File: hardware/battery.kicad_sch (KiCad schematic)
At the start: 10 parts, among them IC1 BQ29732DSER, Q1 CSD16406Q3, Q2 CSD16406Q3

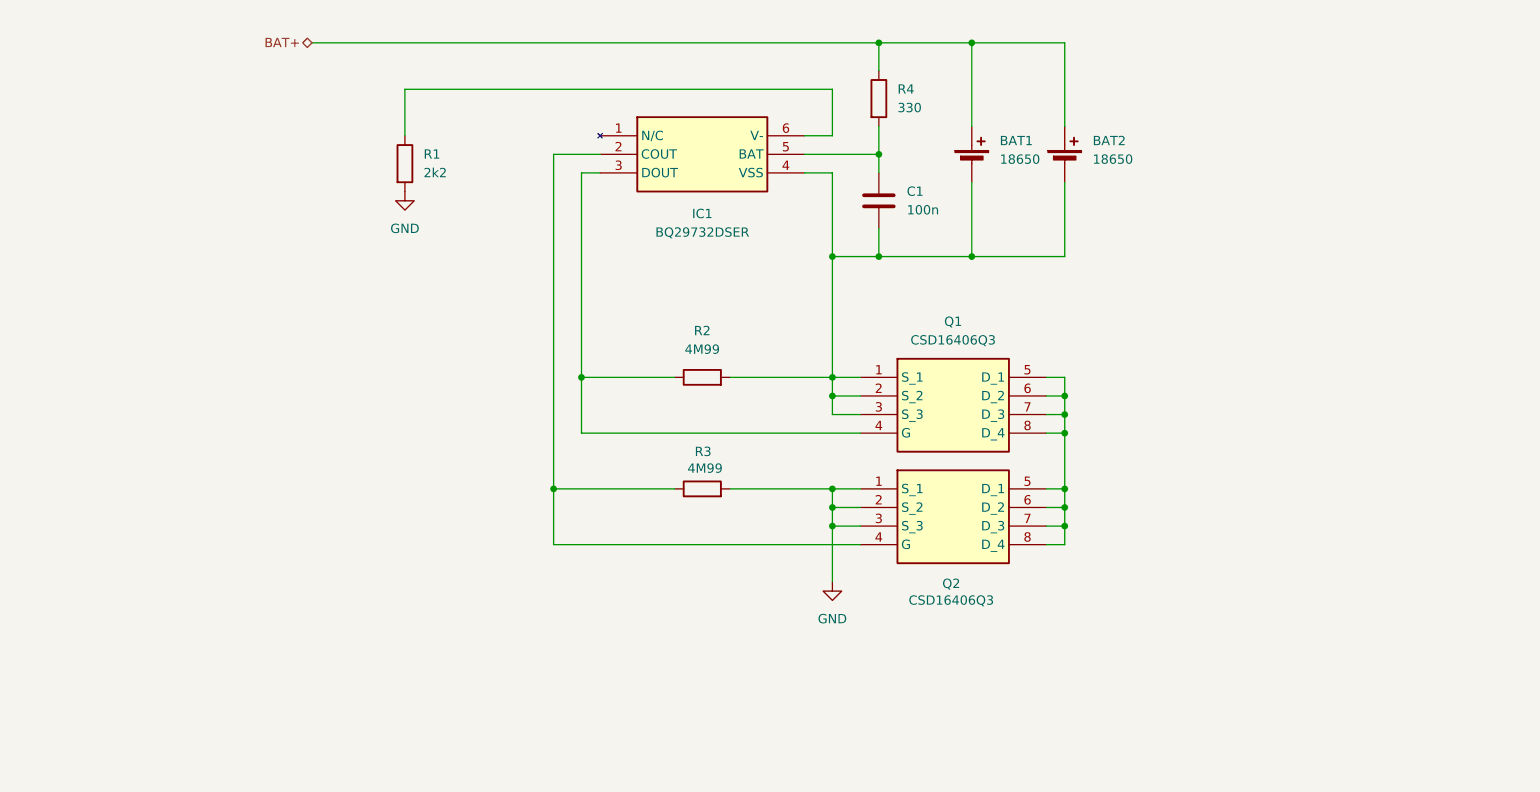
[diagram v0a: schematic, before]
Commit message: Battery temperature meter added to MCU
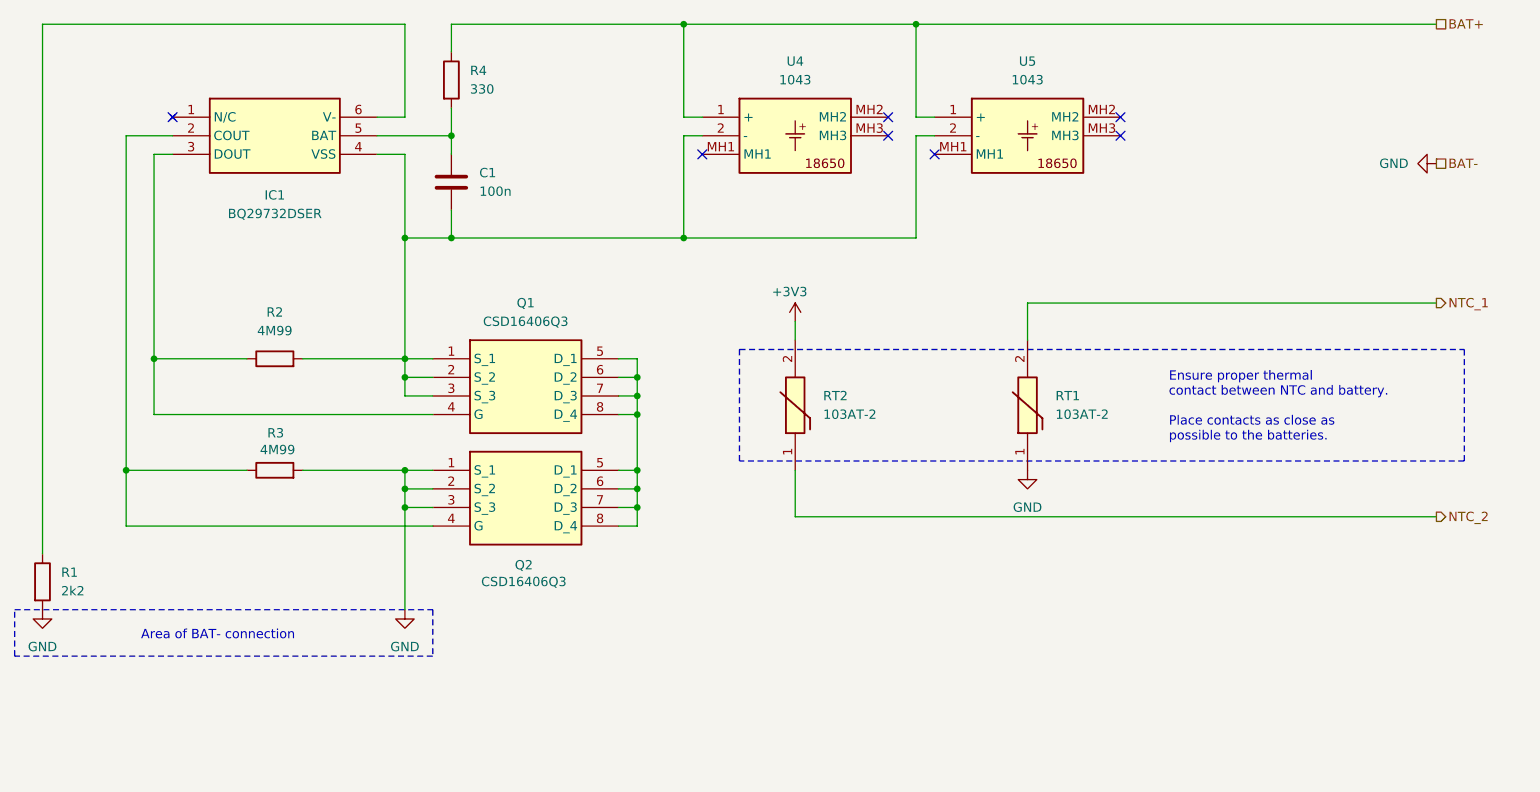
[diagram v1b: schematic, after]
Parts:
- removed BAT1, BAT2: 18650, symbol Device:Battery_Cell
- added RT1, RT2: 103AT-2, 103AT2, symbol SamacSys_Parts:103AT-2
- added U4, U5: 1043, 1043, symbol SamacSys_Parts:1043
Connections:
- net BAT+: now also U4.1 (+), U5.1 (+)
- net GND: now also RT1.1
- net at C1.2, IC1.4 (VSS), Q1.1 (S_1)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: now also U4.2 (-), U5.2 (-)
- new net +3V3: RT2.2
- new net NTC_1: RT1.2
- new net NTC_2: RT2.1
- no-connect marks 0 -> 7
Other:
- note added: "Area of BAT- connection"
- note added: "Ensure proper thermal contact between NTC and battery. Place contacts as close as possible to the batteries."
- moved on the sheet: C1, IC1, Q1, Q2, R1, R2, R3, R4

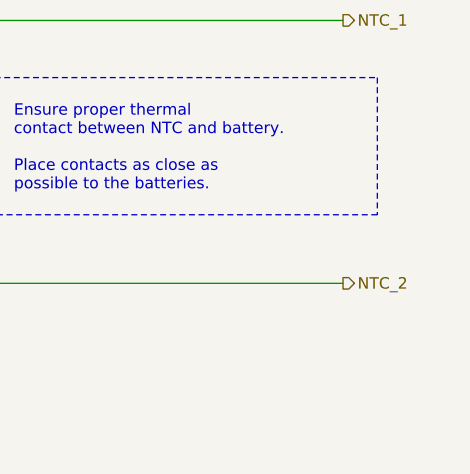
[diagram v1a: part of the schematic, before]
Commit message: Board connector added
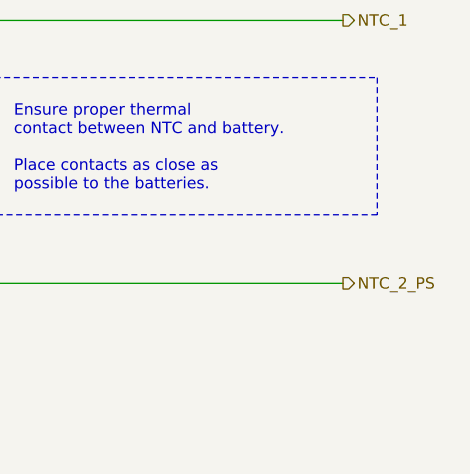
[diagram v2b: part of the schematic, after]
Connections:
- net NTC_2 renamed NTC_2_PS
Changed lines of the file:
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@@
 		)
 	)
-	(hierarchical_label "NTC_2"
+	(hierarchical_label "NTC_2_PS"
 		(shape output)
 		(at 245.11 124.46 0)

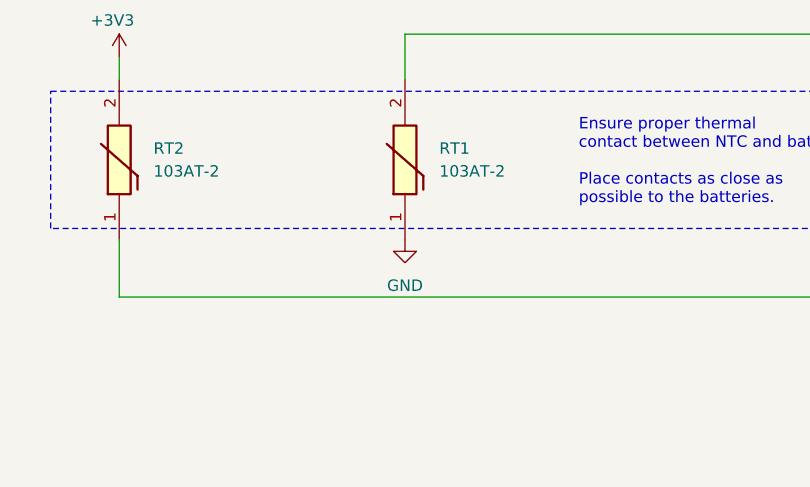
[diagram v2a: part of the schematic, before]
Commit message: Fixed MOS and board connector
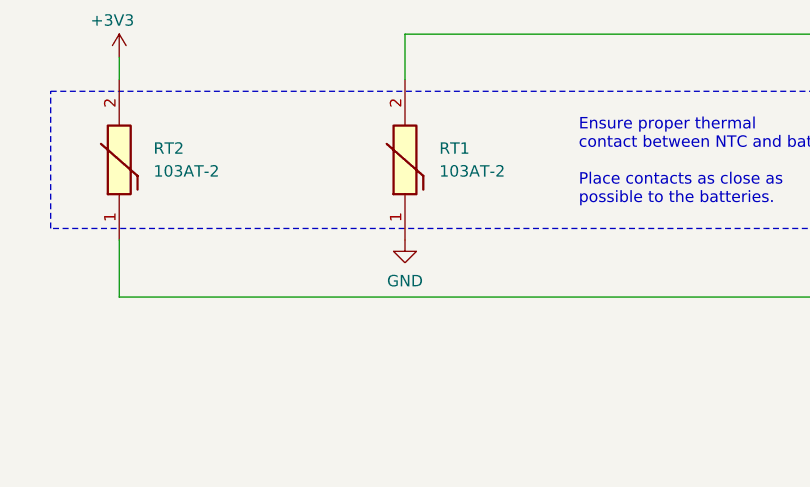
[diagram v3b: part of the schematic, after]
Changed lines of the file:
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@@
 		(on_board yes)
 		(dnp no)
-		(fields_autoplaced yes)
 		(property "Reference" "#PWR073"
 			(at 189.23 124.46 0)
@@
 		)
 		(property "Value" "GND"
-			(at 189.23 123.19 0)
+			(at 189.23 122.682 0)
 			(effects
 				(font

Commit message: prevention save
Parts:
- C1: footprint (none) -> Capacitor_SMD:C_0402_1005Metric
- R1: renamed from R4; footprint Resistor_SMD:R_0805_2012Metric -> Resistor_SMD:R_0603_1608Metric
- R4: renamed from R1; footprint Resistor_SMD:R_0805_2012Metric -> Resistor_SMD:R_0402_1005Metric
- renumbered U4 to BAT1, U5 to BAT2
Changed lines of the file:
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@@
 		(dnp no)
 		(fields_autoplaced yes)
-		(property "Reference" "R1"
+		(property "Reference" "R4"
 			(at 57.15 132.0799 0)
 			(effects
@@
 			)
 		)
-		(property "Footprint" "Resistor_SMD:R_0805_2012Metric"
+		(property "Footprint" "Resistor_SMD:R_0402_1005Metric"
 			(at 52.832 133.35 90)
 			(effects
@@
 			(project "obvod"
 				(path "/e8e834c4-1afb-42f7-b718-3cb720dae1d5/f61c7da5-11ee-4b50-a688-248a75ac3e8f"
-					(reference "R1")
+					(reference "R4")
 					(unit 1)
 				)
@@
 		(dnp no)
 		(fields_autoplaced yes)
-		(property "Reference" "U4"
+		(property "Reference" "BAT1"
 			(at 157.48 62.23 0)
 			(effects
@@
 			(project ""
 				(path "/e8e834c4-1afb-42f7-b718-3cb720dae1d5/f61c7da5-11ee-4b50-a688-248a75ac3e8f"
-					(reference "U4")
+					(reference "BAT1")
 					(unit 1)
 				)
@@
 		(dnp no)
 		(fields_autoplaced yes)
-		(property "Reference" "U5"
+		(property "Reference" "BAT2"
 			(at 189.23 62.23 0)
 			(effects
@@
 			(project "obvod"
 				(path "/e8e834c4-1afb-42f7-b718-3cb720dae1d5/f61c7da5-11ee-4b50-a688-248a75ac3e8f"
-					(reference "U5")
+					(reference "BAT2")
 					(unit 1)
 				)
@@
 			)
 		)
-		(property "Footprint" ""
+		(property "Footprint" "Capacitor_SMD:C_0402_1005Metric"
 			(at 111.4552 82.55 0)
 			(effects
@@
 		(dnp no)
 		(fields_autoplaced yes)
-		(property "Reference" "R4"
+		(property "Reference" "R1"
 			(at 113.03 63.4999 0)
 			(effects
@@
 			)
 		)
-		(property "Footprint" "Resistor_SMD:R_0805_2012Metric"
+		(property "Footprint" "Resistor_SMD:R_0603_1608Metric"
 			(at 108.712 64.77 90)
 			(effects
@@
 			(project "obvod"
 				(path "/e8e834c4-1afb-42f7-b718-3cb720dae1d5/f61c7da5-11ee-4b50-a688-248a75ac3e8f"
-					(reference "R4")
+					(reference "R1")
 					(unit 1)
 				)

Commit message: Revised and completed BOM
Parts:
- R2, R3: footprint Resistor_SMD:R_0805_2012Metric -> Resistor_SMD:R_0402_1005Metric
- renumbered RT1 to NTC1, RT2 to NTC2
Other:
- moved on the sheet: NTC1, NTC2
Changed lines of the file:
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@@
 	(wire
 		(pts
-			(xy 157.48 97.79) (xy 157.48 100.33)
+			(xy 189.23 132.08) (xy 189.23 134.62)
 		)
 		(stroke
@@
 	(wire
 		(pts
+			(xy 189.23 158.75) (xy 245.11 158.75)
+		)
+		(stroke
+			(width 0)
+			(type default)
+		)
+	)
+	(wire
+		(pts
 			(xy 135.89 125.73) (xy 135.89 123.19)
 		)
@@
 	(wire
 		(pts
-			(xy 189.23 95.25) (xy 189.23 100.33)
+			(xy 189.23 93.98) (xy 189.23 99.06)
 		)
 		(stroke
@@
 	(wire
 		(pts
-			(xy 245.11 124.46) (xy 157.48 124.46)
-		)
-		(stroke
-			(width 0)
-			(type default)
-		)
-	)
-	(wire
-		(pts
 			(xy 69.85 102.87) (xy 82.55 102.87)
 		)
@@
 	(wire
 		(pts
-			(xy 245.11 95.25) (xy 189.23 95.25)
+			(xy 245.11 93.98) (xy 189.23 93.98)
 		)
 		(stroke
@@
 	(wire
 		(pts
-			(xy 157.48 124.46) (xy 157.48 118.11)
+			(xy 189.23 158.75) (xy 189.23 152.4)
 		)
 		(stroke
@@
 	)
 	(rectangle
-		(start 149.86 101.6)
-		(end 248.92 116.84)
+		(start 182.88 100.33)
+		(end 248.92 153.67)
 		(stroke
 			(width 0)
@@
 	(text "Ensure proper thermal \ncontact between NTC and battery.\n\nPlace contacts as close as \npossible to the batteries."
 		(exclude_from_sim no)
-		(at 208.534 109.474 0)
+		(at 208.788 127 0)
 		(effects
 			(font
@@
 	(hierarchical_label "NTC_2_PS"
 		(shape output)
-		(at 245.11 124.46 0)
+		(at 245.11 158.75 0)
 		(effects
 			(font
@@
 	(hierarchical_label "NTC_1"
 		(shape output)
-		(at 245.11 95.25 0)
+		(at 245.11 93.98 0)
 		(effects
 			(font
@@
 	(symbol
 		(lib_id "SamacSys_Parts:103AT-2")
-		(at 157.48 118.11 90)
+		(at 189.23 152.4 90)
 		(unit 1)
 		(exclude_from_sim no)
@@
 		(dnp no)
 		(fields_autoplaced yes)
-		(property "Reference" "RT2"
-			(at 161.29 107.9499 90)
+		(property "Reference" "NTC2"
+			(at 193.04 142.2399 90)
 			(effects
 				(font
@@
 		)
 		(property "Value" "103AT-2"
-			(at 161.29 110.4899 90)
+			(at 193.04 144.7799 90)
 			(effects
 				(font
@@
 		)
 		(property "Footprint" "103AT2"
-			(at 253.67 104.14 0)
+			(at 285.42 138.43 0)
 			(effects
 				(font
@@
 		)
 		(property "Datasheet" "https://www.semitec-global.com/uploads/2022/01/P12-13-AT-Thermistor.pdf"
-			(at 353.67 104.14 0)
+			(at 385.42 138.43 0)
 			(effects
 				(font
@@
 		)
 		(property "Description" "NTC (Negative Temperature Coefficient) Thermistors 10kohm 1%"
-			(at 157.48 118.11 0)
+			(at 189.23 152.4 0)
 			(effects
 				(font
@@
 		)
 		(property "Height" "9.5"
-			(at 553.67 104.14 0)
+			(at 585.42 138.43 0)
 			(effects
 				(font
@@
 		)
 		(property "Manufacturer_Name" "Semitec"
-			(at 653.67 104.14 0)
+			(at 685.42 138.43 0)
 			(effects
 				(font
@@
 		)
 		(property "Manufacturer_Part_Number" "103AT-2"
-			(at 753.67 104.14 0)
+			(at 785.42 138.43 0)
 			(effects
 				(font
@@
 		)
 		(property "Mouser Part Number" "954-103AT-2"
-			(at 853.67 104.14 0)
+			(at 885.42 138.43 0)
 			(effects
 				(font
@@
 		)
 		(property "Mouser Price/Stock" "https://www.mouser.co.uk/ProductDetail/Semitec/103AT-2?qs=wgO0AD0o1vvcDzsKguD%252Bew%3D%3D"
-			(at 953.67 104.14 0)
+			(at 985.42 138.43 0)
 			(effects
 				(font
@@
 		)
 		(property "Arrow Part Number" ""
-			(at 1053.67 104.14 0)
+			(at 1085.42 138.43 0)
 			(effects
 				(font
@@
 		)
 		(property "Arrow Price/Stock" ""
-			(at 1153.67 104.14 0)
+			(at 1185.42 138.43 0)
 			(effects
 				(font
@@
 			(project "obvod"
 				(path "/e8e834c4-1afb-42f7-b718-3cb720dae1d5/f61c7da5-11ee-4b50-a688-248a75ac3e8f"
-					(reference "RT2")
+					(reference "NTC2")
 					(unit 1)
 				)
@@
 	(symbol
 		(lib_id "power:GND")
-		(at 189.23 118.11 0)
+		(at 189.23 116.84 0)
 		(unit 1)
 		(exclude_from_sim no)
@@
 		(dnp no)
 		(property "Reference" "#PWR073"
-			(at 189.23 124.46 0)
+			(at 189.23 123.19 0)
 			(effects
 				(font
@@
 		)
 		(property "Value" "GND"
-			(at 189.23 122.682 0)
+			(at 189.23 121.412 0)
 			(effects
 				(font
@@
 		)
 		(property "Footprint" ""
-			(at 189.23 118.11 0)
+			(at 189.23 116.84 0)
 			(effects
 				(font
@@
 		)
 		(property "Datasheet" ""
-			(at 189.23 118.11 0)
+			(at 189.23 116.84 0)
 			(effects
 				(font
@@
 		)
 		(property "Description" "Power symbol creates a global label with name \"GND\" , ground"
-			(at 189.23 118.11 0)
+			(at 189.23 116.84 0)
 			(effects
 				(font
@@
 			)
 		)
-		(property "Footprint" "Resistor_SMD:R_0805_2012Metric"
+		(property "Footprint" "Resistor_SMD:R_0402_1005Metric"
 			(at 86.36 119.888 90)
 			(effects
@@
 	(symbol
 		(lib_id "SamacSys_Parts:103AT-2")
-		(at 189.23 118.11 90)
+		(at 189.23 116.84 90)
 		(unit 1)
 		(exclude_from_sim no)
@@
 		(dnp no)
 		(fields_autoplaced yes)
-		(property "Reference" "RT1"
-			(at 193.04 107.9499 90)
+		(property "Reference" "NTC1"
+			(at 193.04 106.6799 90)
 			(effects
 				(font
@@
 		)
 		(property "Value" "103AT-2"
-			(at 193.04 110.4899 90)
+			(at 193.04 109.2199 90)
 			(effects
 				(font
@@
 		)
 		(property "Footprint" "103AT2"
-			(at 285.42 104.14 0)
+			(at 285.42 102.87 0)
 			(effects
 				(font
@@
 		)
 		(property "Datasheet" "https://www.semitec-global.com/uploads/2022/01/P12-13-AT-Thermistor.pdf"
-			(at 385.42 104.14 0)
+			(at 385.42 102.87 0)
 			(effects
 				(font
@@
 		)
 		(property "Description" "NTC (Negative Temperature Coefficient) Thermistors 10kohm 1%"
-			(at 189.23 118.11 0)
+			(at 189.23 116.84 0)
 			(effects
 				(font
@@
 		)
 		(property "Height" "9.5"
-			(at 585.42 104.14 0)
+			(at 585.42 102.87 0)
 			(effects
 				(font
@@
 		)
 		(property "Manufacturer_Name" "Semitec"
-			(at 685.42 104.14 0)
+			(at 685.42 102.87 0)
 			(effects
 				(font
@@
 		)
 		(property "Manufacturer_Part_Number" "103AT-2"
-			(at 785.42 104.14 0)
+			(at 785.42 102.87 0)
 			(effects
 				(font
@@
 		)
 		(property "Mouser Part Number" "954-103AT-2"
-			(at 885.42 104.14 0)
+			(at 885.42 102.87 0)
 			(effects
 				(font
@@
 		)
 		(property "Mouser Price/Stock" "https://www.mouser.co.uk/ProductDetail/Semitec/103AT-2?qs=wgO0AD0o1vvcDzsKguD%252Bew%3D%3D"
-			(at 985.42 104.14 0)
+			(at 985.42 102.87 0)
 			(effects
 				(font
@@
 		)
 		(property "Arrow Part Number" ""
-			(at 1085.42 104.14 0)
+			(at 1085.42 102.87 0)
 			(effects
 				(font
@@
 		)
 		(property "Arrow Price/Stock" ""
-			(at 1185.42 104.14 0)
+			(at 1185.42 102.87 0)
 			(effects
 				(font
@@
 			(project "obvod"
 				(path "/e8e834c4-1afb-42f7-b718-3cb720dae1d5/f61c7da5-11ee-4b50-a688-248a75ac3e8f"
-					(reference "RT1")
+					(reference "NTC1")
 					(unit 1)
 				)
@@
 			)
 		)
-		(property "Footprint" "Resistor_SMD:R_0805_2012Metric"
+		(property "Footprint" "Resistor_SMD:R_0402_1005Metric"
 			(at 86.36 104.648 90)
 			(effects
@@
 	(symbol
 		(lib_id "power:+3V3")
-		(at 157.48 97.79 0)
+		(at 189.23 132.08 0)
 		(unit 1)
 		(exclude_from_sim no)
@@
 		(dnp no)
 		(property "Reference" "#PWR072"
-			(at 157.48 101.6 0)
+			(at 189.23 135.89 0)
 			(effects
 				(font
@@
 		)
 		(property "Value" "+3V3"
-			(at 156.718 93.726 0)
+			(at 188.468 128.016 0)
 			(effects
 				(font
@@
 		)
 		(property "Footprint" ""
-			(at 157.48 97.79 0)
+			(at 189.23 132.08 0)
 			(effects
 				(font
@@
 		)
 		(property "Datasheet" ""
-			(at 157.48 97.79 0)
+			(at 189.23 132.08 0)
 			(effects
 				(font
@@
 		)
 		(property "Description" "Power symbol creates a global label with name \"+3V3\""
-			(at 157.48 97.79 0)
-			(effects
-				(font
+			(at 189.23 132.08 0)
+			(effects
+				(font
